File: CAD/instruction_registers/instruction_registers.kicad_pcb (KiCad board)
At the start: 2 copper layers, 100 x 60 mm, 59 parts, among them J1 Conn_01x32_Pin, J2 Conn_01x06_Pin, SW1 SW_Push, SW2 SW_Push, SW3 SW_SPDT, U1 74HC377, U2 74HC377, U3 74HC377, U4 74HC245, U5 74HC245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

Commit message: update IR, move crystal, change capacitors, add testpoints, ground planes
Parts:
- added JP1: SolderJumper_2_Open, Jumper:SolderJumper-2_P1.3mm_Open_RoundedPad1.0x1.5mm, F.Cu at (94.7, 55.4)
- added TP5: TestPoint, TestPoint:TestPoint_THTPad_D1.0mm_Drill0.5mm, F.Cu at (97.7, 72.3)
- added TP6: TestPoint, TestPoint:TestPoint_THTPad_D1.0mm_Drill0.5mm, F.Cu at (94.7, 67.1)
- added TP7: TestPoint, TestPoint:TestPoint_THTPad_D1.0mm_Drill0.5mm, F.Cu at (91.7, 72.3)
- C10, C11: value 22pF -> 12pF
- D5: value IR2_OUT -> IR3_OUT
- moved C10 5.11 mm to (101.7, 72.0), turned to 0 degrees
- moved Y1 2.10 mm to (97.5, 69.2)
- moved R4 1.60 mm to (91.6, 55.3), turned to 90 degrees
- moved C11 0.43 mm to (93.9, 70.5), turned to -90 degrees
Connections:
- net Net-(U9-XTAL1/PB6) renamed /xtal1
- net Net-(U9-XTAL2/PB7) renamed /xtal2
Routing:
- net /lcd.bl+: track 10.0 -> 12.4 mm
- net /xtal1: track 8.33 -> 10.6 mm
- net Net-(JP1-A): track 12.7 -> 14.9 mm
- net /xtal2: track 8.38 -> 9.90 mm
- net ~{pl}: track 65.9 -> 67.3 mm
- net ~{ir2_in}: track 119.1 -> 120.1 mm
- net ~{ir2_out}: track 120.8 -> 121.6 mm
- net ~{sw_mode}: track 28.4 -> 27.8 mm
- net GND: vias 151 -> 147
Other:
- board text added: "+"
- board text added: "INSTSRUCTION REGISTERS"
- board text added: "XTAL1"
- board text added: "XTAL2"

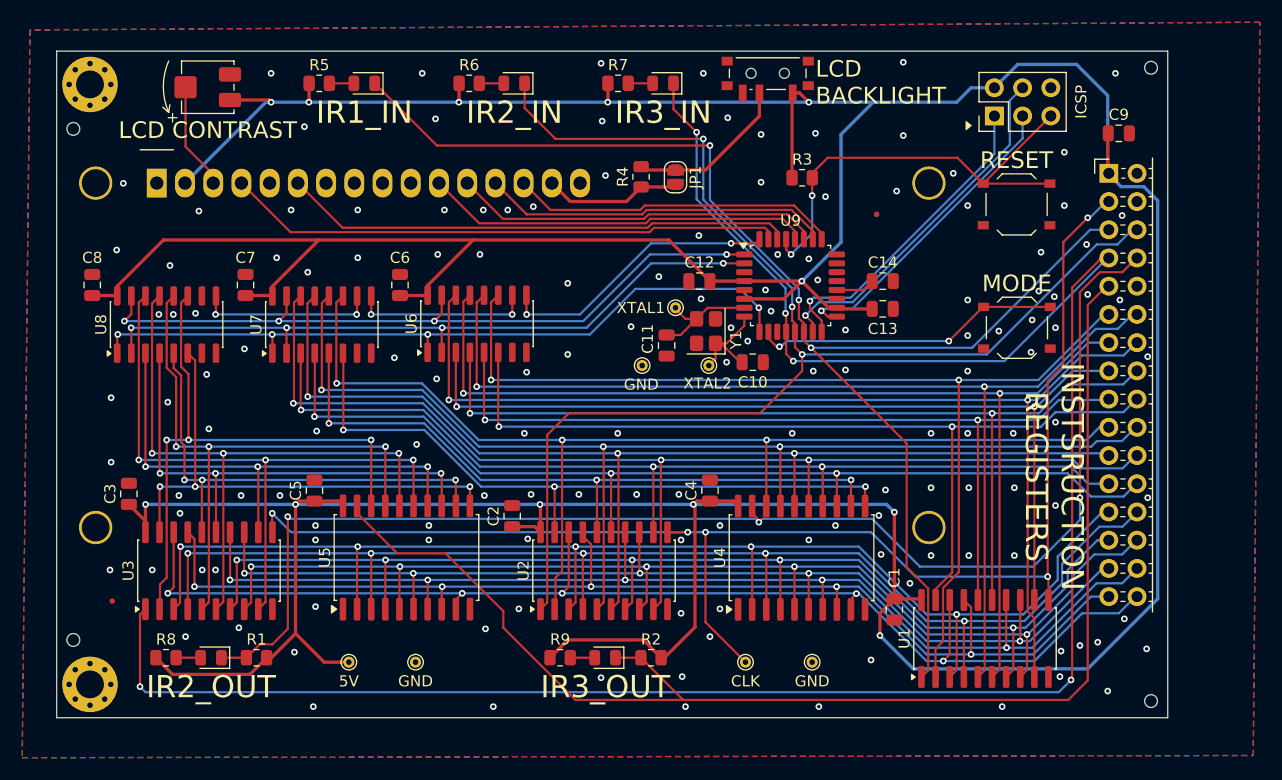
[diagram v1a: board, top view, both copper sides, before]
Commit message: IR layout changes
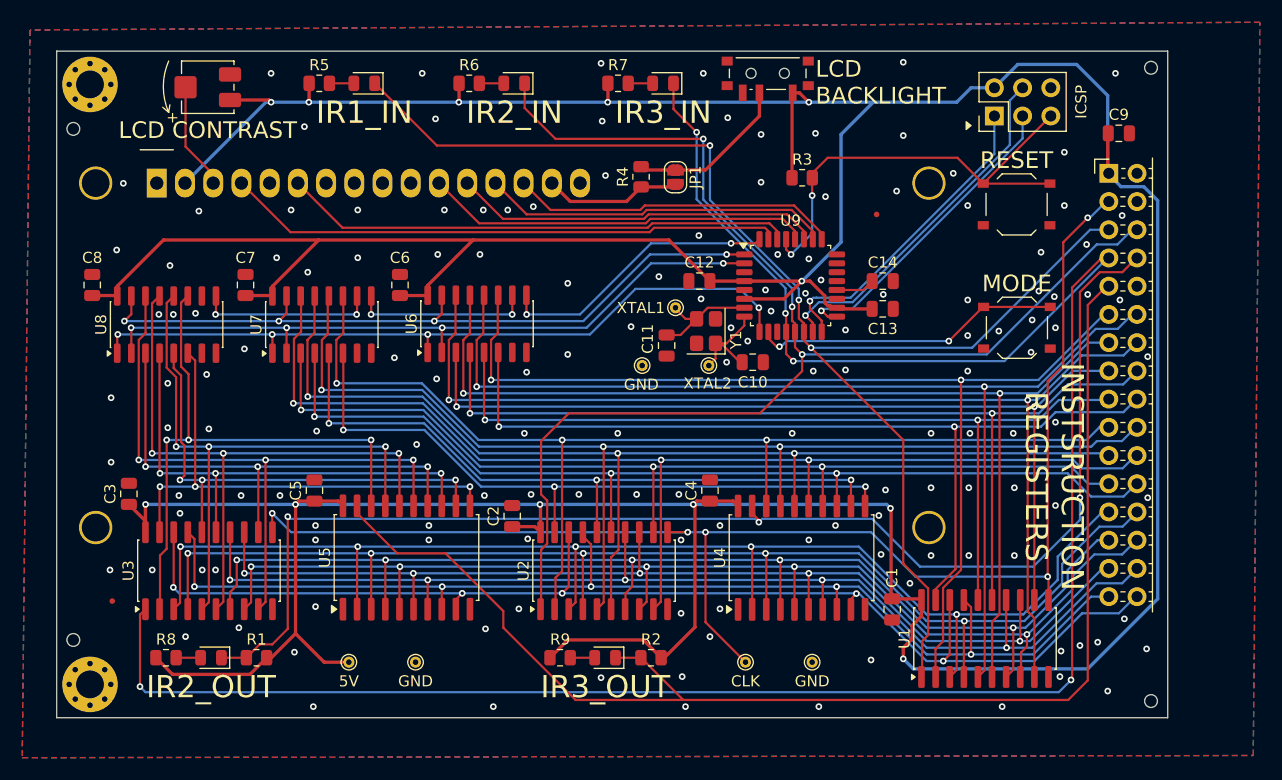
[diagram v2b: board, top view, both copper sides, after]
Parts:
- moved C1 0.20 mm to (114.2, 94.2)
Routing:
- net /dbus7: track 112.6 -> 111.6 mm
- net /q3.6: track 43.3 -> 43.8 mm
- net GND: vias 147 -> 150

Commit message: IR layout changes
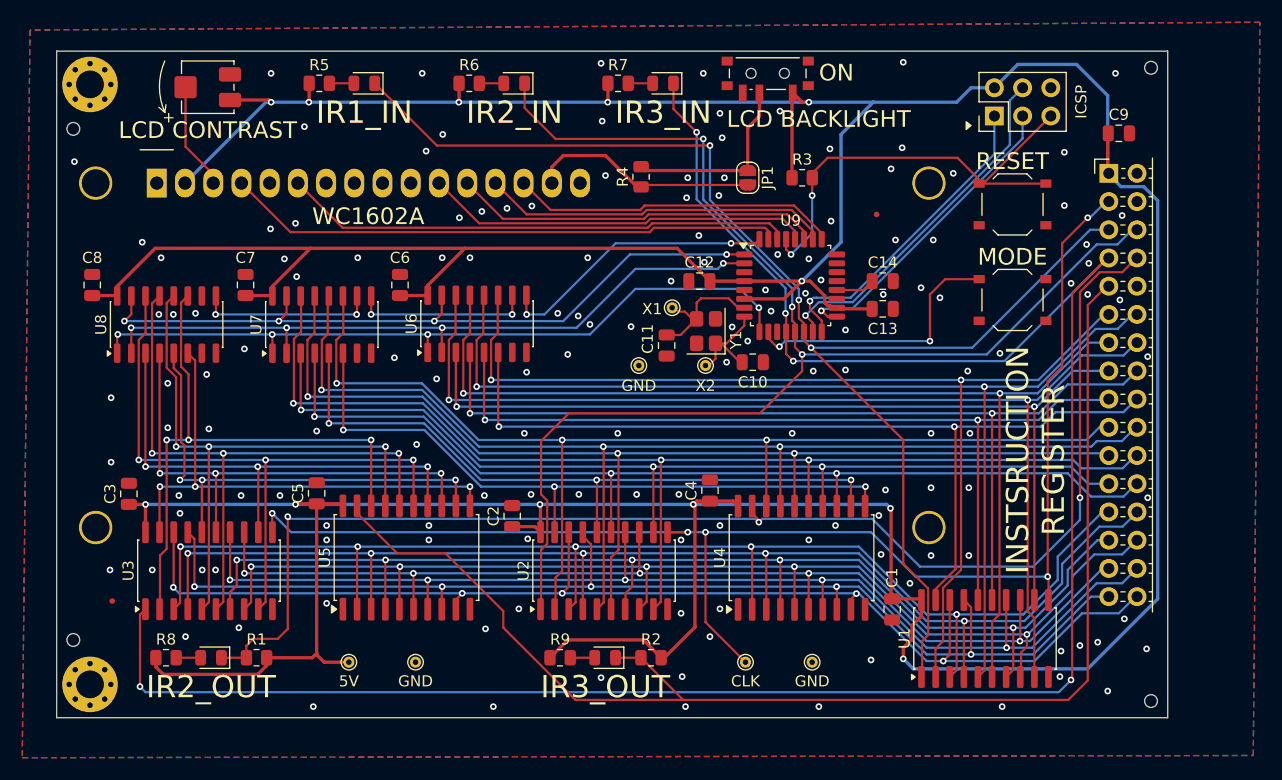
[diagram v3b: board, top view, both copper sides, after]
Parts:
- moved JP1 6.50 mm to (101.2, 55.4)
- moved SW2 2.53 mm to (125.0, 66.4)
- moved SW1 0.37 mm to (125.0, 57.8)
- moved C5 0.32 mm to (62.4, 83.8)
- moved TP5 0.30 mm to (97.4, 72.3)
- moved TP6 0.30 mm to (94.4, 67.1)
- moved TP7 0.30 mm to (91.4, 72.3)
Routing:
- net /lcd.bl+: track 12.4 -> 20.1 mm
- net +5V: track 467.5 -> 462.4 mm
- net ~{sw_mode}: track 27.8 -> 24.7 mm
- net Net-(JP1-A): track 14.9 -> 16.7 mm
- net /xtal2: track 9.90 -> 8.71 mm
- net /dbus7: track 111.6 -> 110.6 mm
- net ~{ir3_out}: track 119.1 -> 118.2 mm
- net ~{ir2_out}: track 121.6 -> 120.8 mm
- net /lcd.v_{o}: track 9.66 -> 8.87 mm
- net /q2.2: track 102.7 -> 102.0 mm
- net ~{ir3_in}: track 193.1 -> 192.3 mm
- net /dbus2: track 108.7 -> 108.0 mm
- net /dbus0: track 120.1 -> 119.6 mm
- net /lcd.d7: track 29.6 -> 29.0 mm
- net /dbus4: track 100.7 -> 100.1 mm
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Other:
- board text added: "INSTSRUCTION REGISTER"
- board text added: "ON"
- board text added: "WC1602A"
- board text added: "X1"
- board text added: "X2"
- board text removed: "INSTSRUCTION REGISTERS"
- board text removed: "XTAL1"
- board text removed: "XTAL2"
